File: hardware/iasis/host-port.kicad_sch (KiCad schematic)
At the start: 17 parts, among them J901 1054500101, U901 TPD4E02B04DQAR, U902 TPD4E02B04DQAR, U903 HD3SS3212IRKSR, U904 TPD6S300ARUKR, U905 FUSB302BMPX

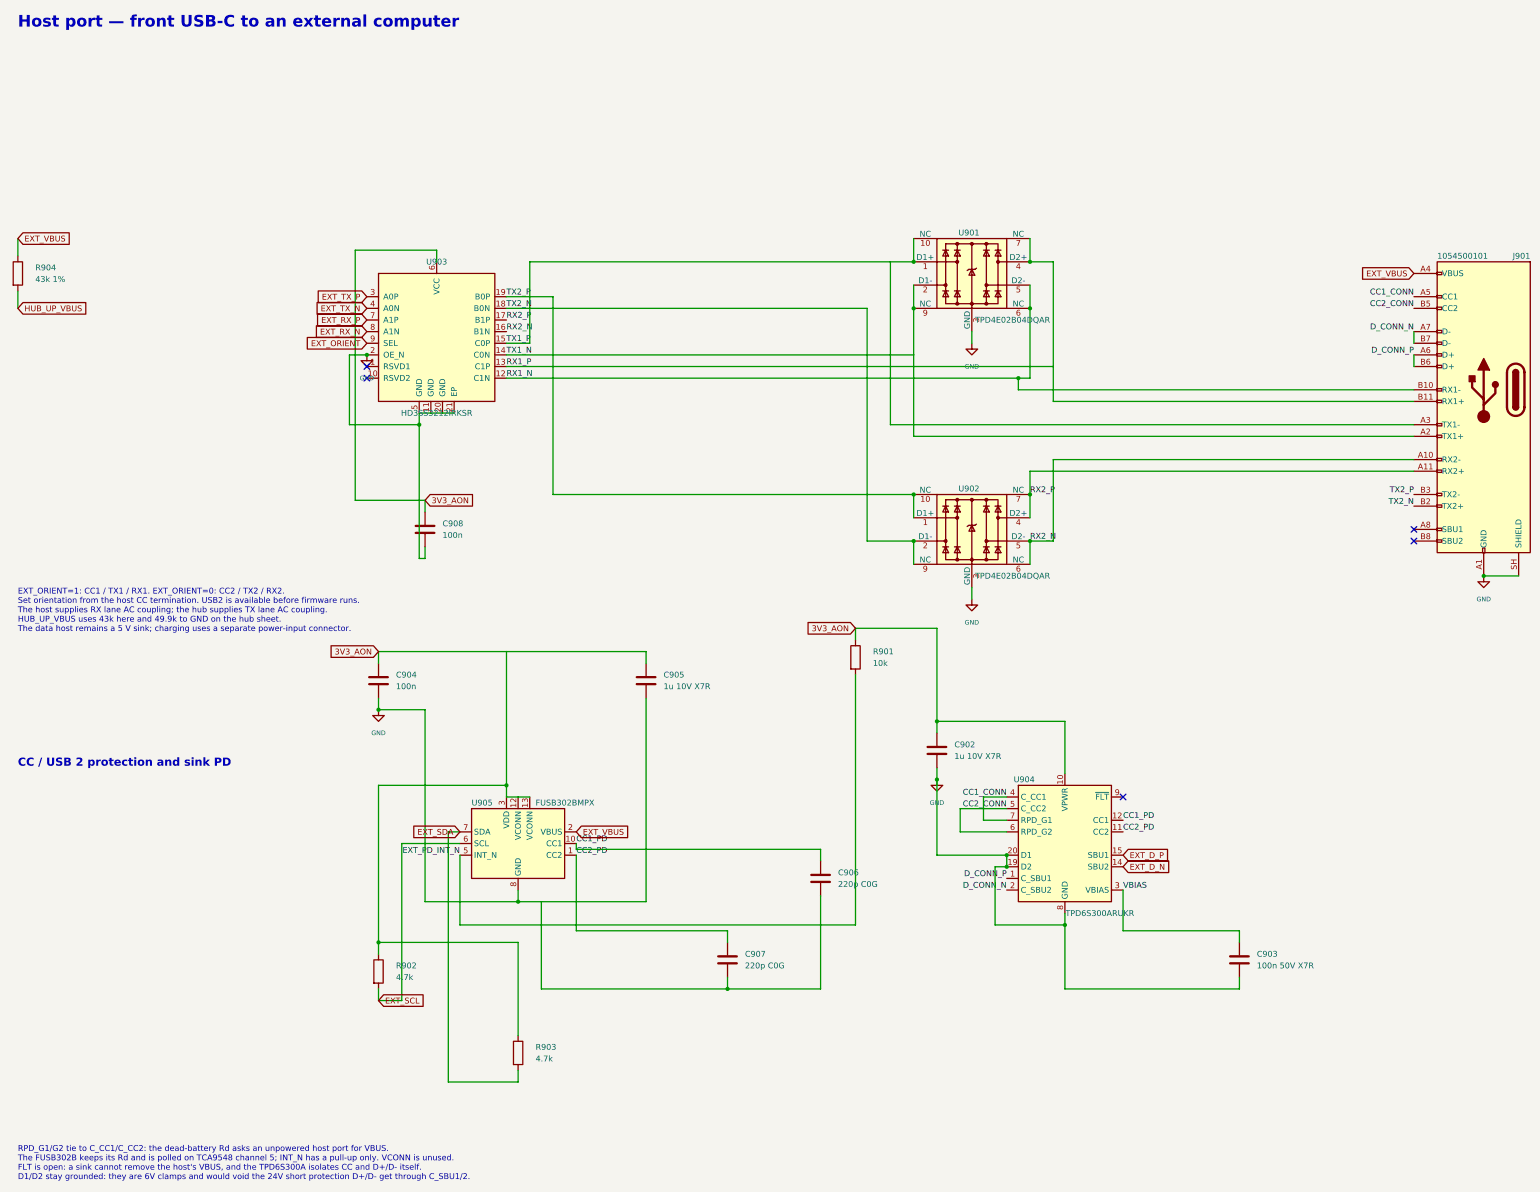
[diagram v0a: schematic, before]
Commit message: Add the CM5 carrier design for reference
The first board revision: a Raspberry Pi CM5 carrier with M.2 NVMe,
Ethernet and five USB 3 and USB-PD ports, as it stood before the compact
hub replaced it, squashed from 45 commits.
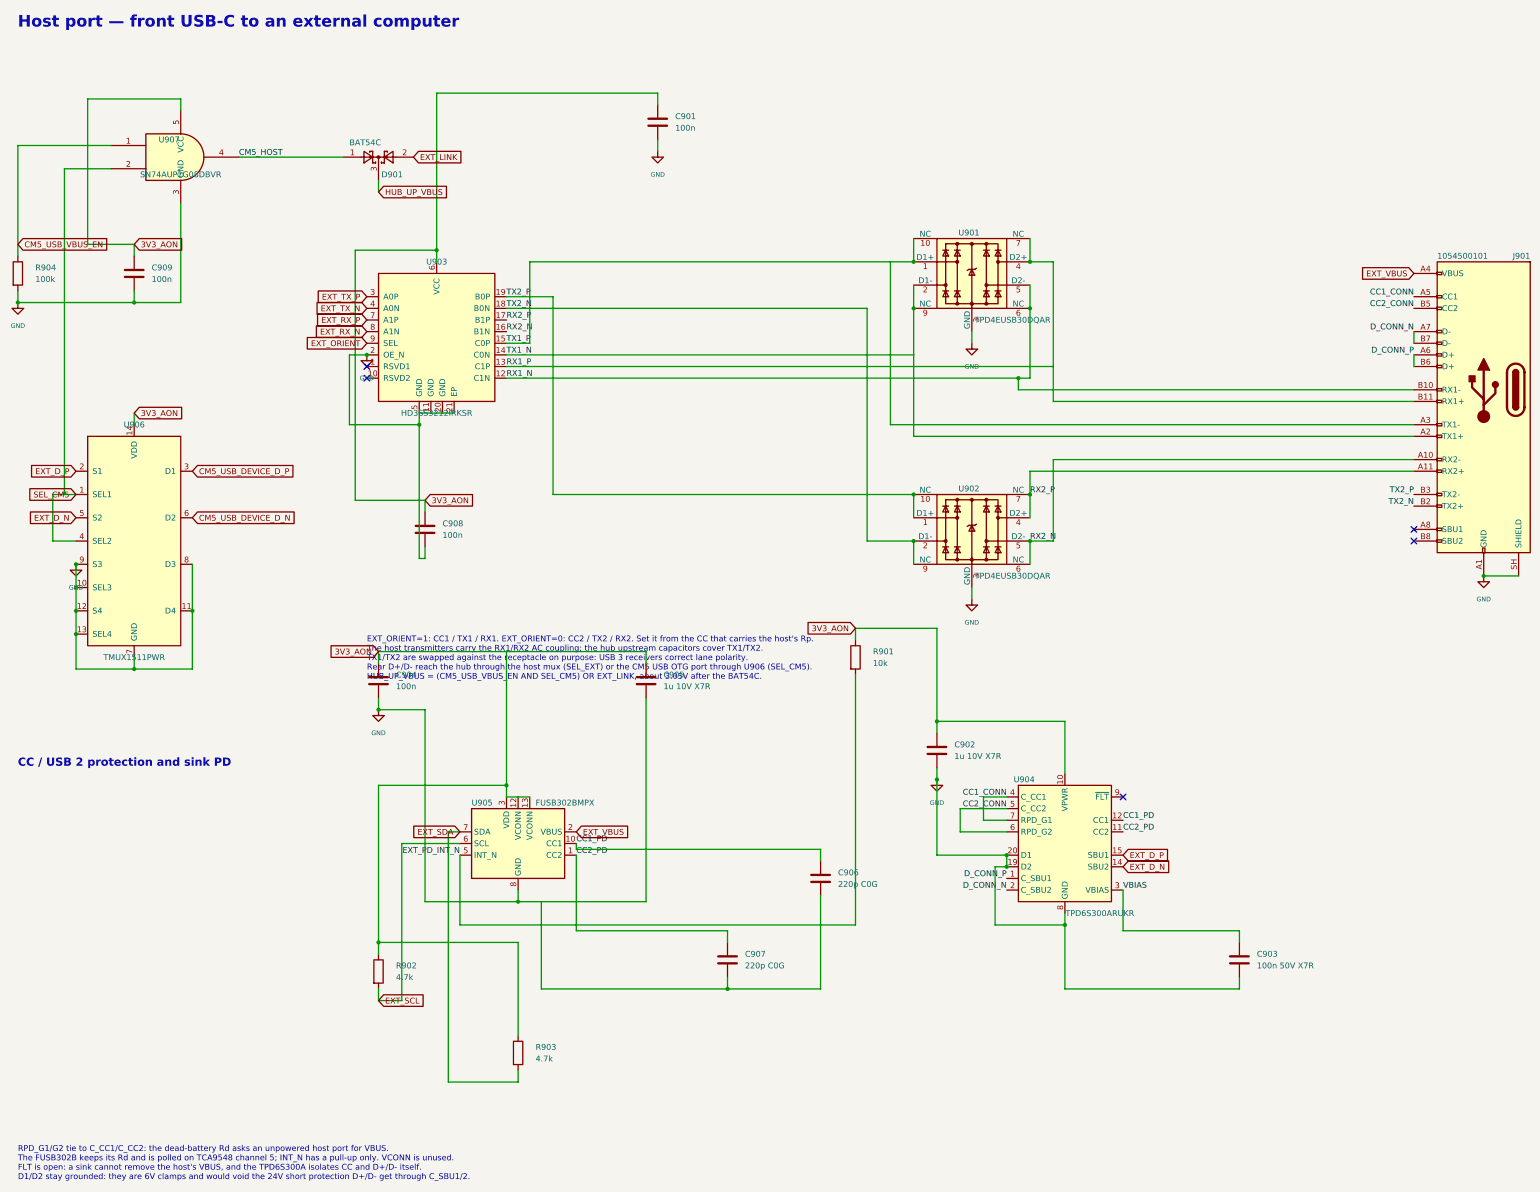
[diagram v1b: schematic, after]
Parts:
- added C901, C909: 100n, Capacitor_SMD:C_0402_1005Metric, symbol Device:C
- added D901: BAT54C, Package_TO_SOT_SMD:SOT-23, symbol Diode:BAT54C
- added U906: TMUX1511PWR, Package_SO:TSSOP-14_4.4x5mm_P0.65mm, symbol Iasis:TMUX1511PWR
- added U907: SN74AUP1G08DBVR, Package_TO_SOT_SMD:SOT-23-5, symbol 74xGxx:74AUP1G08
- C902, C905: LCSC C22399625 -> (none); MPN CGA0603X7R105K100JT -> (none); Manufacturer HRE -> (none)
- C903: LCSC C14663 -> (none); MPN CC0603KRX7R9BB104 -> (none); Manufacturer YAGEO -> (none)
- C904, C908: LCSC C1525 -> (none); MPN CL05B104KO5NNNC -> (none); Manufacturer Samsung Electro-Mechanics -> (none)
- C906, C907: LCSC C39122 -> (none); MPN 0402CG221J500NT -> (none); Manufacturer FH (Guangdong Fenghua Advanced Tech) -> (none)
- J901: Manufacturer MOLEX -> Molex
- R901: LCSC C25744 -> (none); MPN 0402WGF1002TCE -> (none); Manufacturer UNI-ROYAL(Uniroyal Elec) -> (none)
- R902, R903: LCSC C25900 -> (none); MPN 0402WGF4701TCE -> (none); Manufacturer UNI-ROYAL(Uniroyal Elec) -> (none)
- R904: value 43k 1% -> 100k; LCSC C8329 -> (none); MPN 0402WGF4302TCE -> (none); Manufacturer UNI-ROYAL(Uniroyal Elec) -> (none)
- U901, U902: value TPD4E02B04DQAR -> TPD4EUSB30DQAR; symbol Iasis:TPD4E02B04DQA -> Power_Protection:TPD4EUSB30; LCSC C106794 -> C90627; MPN TPD4E02B04DQAR -> TPD4EUSB30DQAR
- U904: LCSC C2876380 -> (none); MPN TPD6S300ARUKR -> (none); Manufacturer Texas Instruments -> (none)
- U905: LCSC C132291 -> (none); MPN FUSB302BMPX -> (none); Manufacturer onsemi -> (none)
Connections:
- net 3V3_AON: now also C901.1, C909.1, U906.14 (VDD), U907.5 (VCC)
- net EXT_D_N: now also U906.5 (S2)
- net EXT_D_P: now also U906.2 (S1)
- net EXT_VBUS: no longer R904.1
- net GND: now also R904.2, C901.2, C909.2, U906.10 (SEL3), U906.11 (D4), U906.12 (S4), U906.13 (SEL4), U906.7 (GND), U906.8 (D3), U906.9 (S3), U907.3 (GND)
- net HUB_UP_VBUS: now also D901.3; no longer R904.2
- new net CM5_HOST: D901.1, U907.4
- new net CM5_USB_DEVICE_D_N: U906.6 (D2)
- new net CM5_USB_DEVICE_D_P: U906.3 (D1)
- new net CM5_USB_VBUS_EN: R904.1, U907.1
- new net EXT_LINK: D901.2
- new net SEL_CM5: U906.1 (SEL1), U906.4 (SEL2), U907.2
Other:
- note added: "EXT_ORIENT=1: CC1 / TX1 / RX1. EXT_ORIENT=0: CC2 / TX2 / RX2. Set it from the CC that carries the host's Rp. The host transmitters carry the RX1/RX2 AC coupling; the hub upstream capacitors cover TX1/TX2. TX1/TX2 are swapped against the receptacle on purpose: USB 3 receivers correct lane polarity. Rear D+/D- reach the hub through the host mux (SEL_EXT) or the CM5 USB OTG port through U906 (SEL_CM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"
- note removed: "EXT_ORIENT=1: CC1 / TX1 / RX1. EXT_ORIENT=0: CC2 / TX2 / RX2. Set orientation from the host CC termination. USB2 is available before firmware runs. The host supplies RX lane AC coupling; the hub supplies TX lane AC coupling. HUB_UP_VBUS uses 43k here and 49.9k to GND on the hub sheet. The data host remains a 5 V sink; charging uses a separate power-input connector."
